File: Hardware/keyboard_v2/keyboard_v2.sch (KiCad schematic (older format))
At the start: 21 parts, among them J1 Conn_01x08_Male, SW1 SW_Push, SW2 SW_Push, SW3 SW_Push, SW4 SW_Push, SW5 SW_Push, SW6 SW_Push, U1 74HC14

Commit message: Распаян модуль keyboard_v2/
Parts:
- C2, C3, C4, C5, C6, C7: footprint Capacitor_SMD:C_0805_2012Metric_Pad1.18x1.45mm_HandSolder -> Capacitor_SMD:C_1206_3216Metric_Pad1.33x1.80mm_HandSolder
- SW1, SW2, SW3, SW4, SW5, SW6: footprint Button_Switch_SMD:SW_SPST_SMD_6.4_3.7 -> Button_Switch_SMD:SW_SPST_SMD_6.4_3.7_v2
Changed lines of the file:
@@
 F 0 "C2" H 3665 2046 50  0000 L CNN
 F 1 "C" H 3665 1955 50  0000 L CNN
-F 2 "Capacitor_SMD:C_0805_2012Metric_Pad1.18x1.45mm_HandSolder" H 3588 1850 50  0001 C CNN
+F 2 "Capacitor_SMD:C_1206_3216Metric_Pad1.33x1.80mm_HandSolder" H 3588 1850 50  0001 C CNN
 F 3 "~" H 3550 2000 50  0001 C CNN
 	1    3550 2000
@@
 F 0 "C3" H 3665 3546 50  0000 L CNN
 F 1 "C" H 3665 3455 50  0000 L CNN
-F 2 "Capacitor_SMD:C_0805_2012Metric_Pad1.18x1.45mm_HandSolder" H 3588 3350 50  0001 C CNN
+F 2 "Capacitor_SMD:C_1206_3216Metric_Pad1.33x1.80mm_HandSolder" H 3588 3350 50  0001 C CNN
 F 3 "~" H 3550 3500 50  0001 C CNN
 	1    3550 3500
@@
 F 0 "C4" H 3665 5146 50  0000 L CNN
 F 1 "C" H 3665 5055 50  0000 L CNN
-F 2 "Capacitor_SMD:C_0805_2012Metric_Pad1.18x1.45mm_HandSolder" H 3588 4950 50  0001 C CNN
+F 2 "Capacitor_SMD:C_1206_3216Metric_Pad1.33x1.80mm_HandSolder" H 3588 4950 50  0001 C CNN
 F 3 "~" H 3550 5100 50  0001 C CNN
 	1    3550 5100
@@
 F 0 "C5" H 6115 2046 50  0000 L CNN
 F 1 "C" H 6115 1955 50  0000 L CNN
-F 2 "Capacitor_SMD:C_0805_2012Metric_Pad1.18x1.45mm_HandSolder" H 6038 1850 50  0001 C CNN
+F 2 "Capacitor_SMD:C_1206_3216Metric_Pad1.33x1.80mm_HandSolder" H 6038 1850 50  0001 C CNN
 F 3 "~" H 6000 2000 50  0001 C CNN
 	1    6000 2000
@@
 F 0 "C6" H 6115 3546 50  0000 L CNN
 F 1 "C" H 6115 3455 50  0000 L CNN
-F 2 "Capacitor_SMD:C_0805_2012Metric_Pad1.18x1.45mm_HandSolder" H 6038 3350 50  0001 C CNN
+F 2 "Capacitor_SMD:C_1206_3216Metric_Pad1.33x1.80mm_HandSolder" H 6038 3350 50  0001 C CNN
 F 3 "~" H 6000 3500 50  0001 C CNN
 	1    6000 3500
@@
 F 0 "C7" H 6115 5046 50  0000 L CNN
 F 1 "C" H 6115 4955 50  0000 L CNN
-F 2 "Capacitor_SMD:C_0805_2012Metric_Pad1.18x1.45mm_HandSolder" H 6038 4850 50  0001 C CNN
+F 2 "Capacitor_SMD:C_1206_3216Metric_Pad1.33x1.80mm_HandSolder" H 6038 4850 50  0001 C CNN
 F 3 "~" H 6000 5000 50  0001 C CNN
 	1    6000 5000
@@
 F 0 "SW1" V 3804 2098 50  0000 L CNN
 F 1 "SW_Push" V 3895 2098 50  0000 L CNN
-F 2 "Button_Switch_SMD:SW_SPST_SMD_6.4_3.7" H 3850 2150 50  0001 C CNN
+F 2 "Button_Switch_SMD:SW_SPST_SMD_6.4_3.7_v2" H 3850 2150 50  0001 C CNN
 F 3 "~" H 3850 2150 50  0001 C CNN
 	1    3850 1950
@@
 F 0 "SW2" V 3804 3548 50  0000 L CNN
 F 1 "SW_Push" V 3895 3548 50  0000 L CNN
-F 2 "Button_Switch_SMD:SW_SPST_SMD_6.4_3.7" H 3850 3600 50  0001 C CNN
+F 2 "Button_Switch_SMD:SW_SPST_SMD_6.4_3.7_v2" H 3850 3600 50  0001 C CNN
 F 3 "~" H 3850 3600 50  0001 C CNN
 	1    3850 3400
@@
 F 0 "SW3" V 3804 5148 50  0000 L CNN
 F 1 "SW_Push" V 3895 5148 50  0000 L CNN
-F 2 "Button_Switch_SMD:SW_SPST_SMD_6.4_3.7" H 3850 5200 50  0001 C CNN
+F 2 "Button_Switch_SMD:SW_SPST_SMD_6.4_3.7_v2" H 3850 5200 50  0001 C CNN
 F 3 "~" H 3850 5200 50  0001 C CNN
 	1    3850 5000
@@
 F 0 "SW4" V 6254 2048 50  0000 L CNN
 F 1 "SW_Push" V 6345 2048 50  0000 L CNN
-F 2 "Button_Switch_SMD:SW_SPST_SMD_6.4_3.7" H 6300 2100 50  0001 C CNN
+F 2 "Button_Switch_SMD:SW_SPST_SMD_6.4_3.7_v2" H 6300 2100 50  0001 C CNN
 F 3 "~" H 6300 2100 50  0001 C CNN
 	1    6300 1900
@@
 F 0 "SW5" V 6254 3548 50  0000 L CNN
 F 1 "SW_Push" V 6345 3548 50  0000 L CNN
-F 2 "Button_Switch_SMD:SW_SPST_SMD_6.4_3.7" H 6300 3600 50  0001 C CNN
+F 2 "Button_Switch_SMD:SW_SPST_SMD_6.4_3.7_v2" H 6300 3600 50  0001 C CNN
 F 3 "~" H 6300 3600 50  0001 C CNN
 	1    6300 3400
@@
 F 0 "SW6" V 6254 5048 50  0000 L CNN
 F 1 "SW_Push" V 6345 5048 50  0000 L CNN
-F 2 "Button_Switch_SMD:SW_SPST_SMD_6.4_3.7" H 6300 5100 50  0001 C CNN
+F 2 "Button_Switch_SMD:SW_SPST_SMD_6.4_3.7_v2" H 6300 5100 50  0001 C CNN
 F 3 "~" H 6300 5100 50  0001 C CNN
 	1    6300 4900

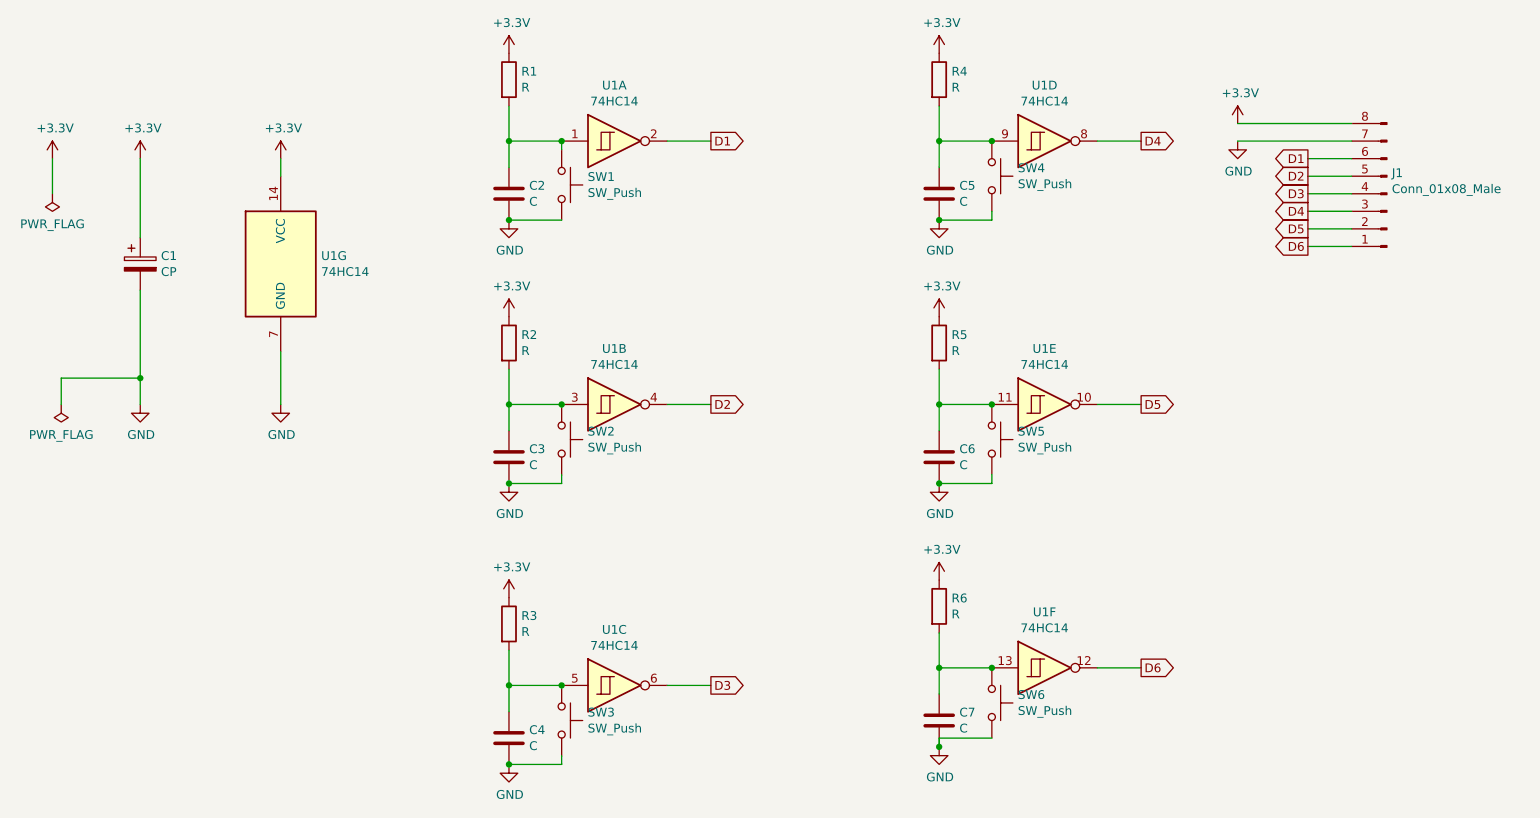
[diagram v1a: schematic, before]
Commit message: Распаян и протестирован модуль клавиатуры keyboard_v3/. Можно приступить к доработке основного приложения
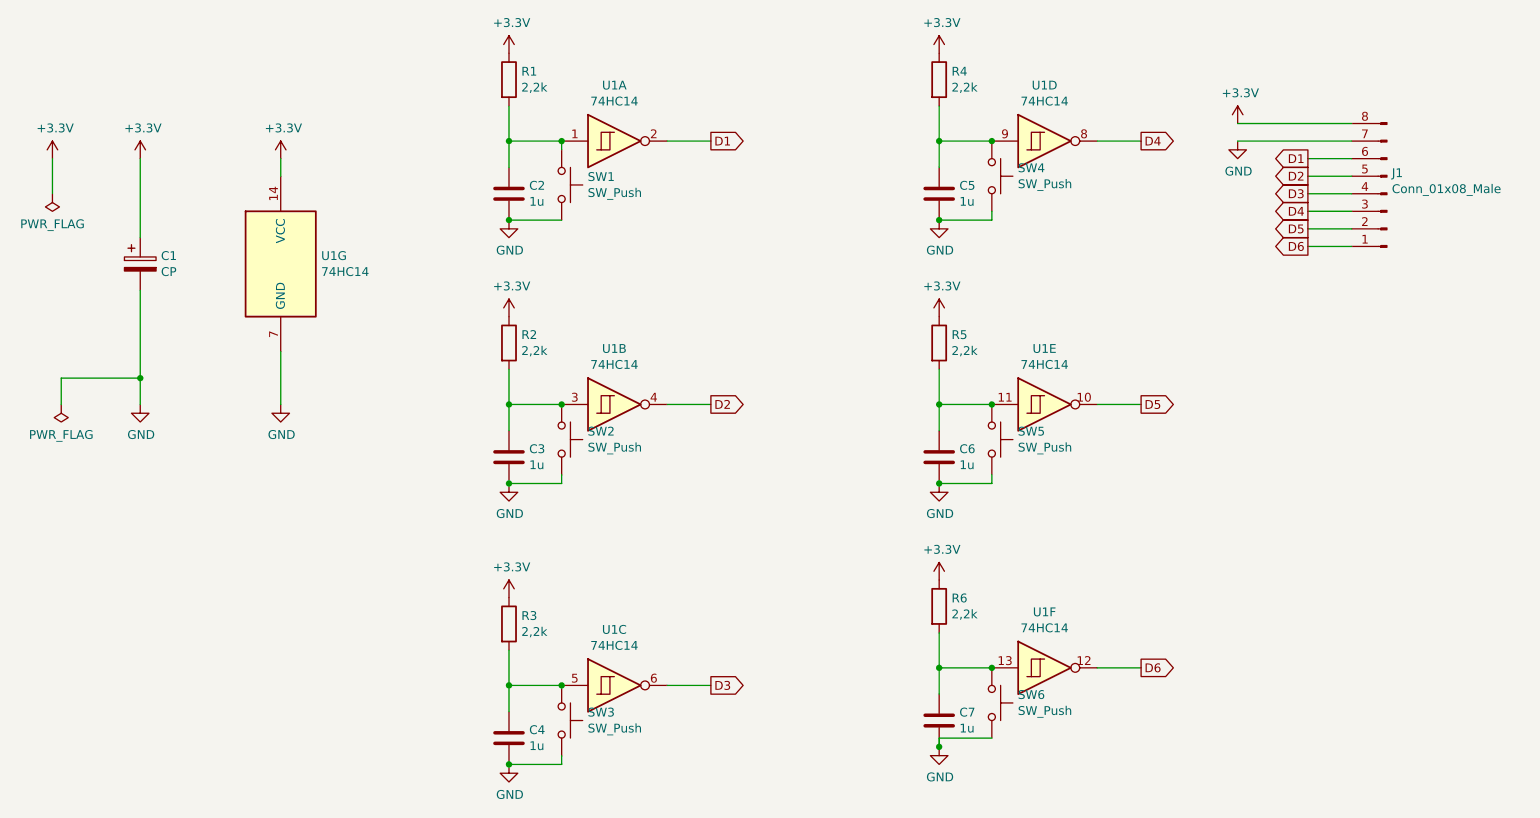
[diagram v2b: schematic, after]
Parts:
- C2, C3, C4, C5, C6, C7: value C -> 1u
- R1, R2, R3, R4, R5, R6: value R -> 2,2k
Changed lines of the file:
@@
 P 3550 1350
 F 0 "R1" H 3620 1396 50  0000 L CNN
-F 1 "R" H 3620 1305 50  0000 L CNN
+F 1 "2,2k" H 3620 1305 50  0000 L CNN
 F 2 "Resistor_SMD:R_1206_3216Metric_Pad1.30x1.75mm_HandSolder" V 3480 1350 50  0001 C CNN
 F 3 "~" H 3550 1350 50  0001 C CNN
@@
 P 3550 2000
 F 0 "C2" H 3665 2046 50  0000 L CNN
-F 1 "C" H 3665 1955 50  0000 L CNN
+F 1 "1u" H 3665 1955 50  0000 L CNN
 F 2 "Capacitor_SMD:C_1206_3216Metric_Pad1.33x1.80mm_HandSolder" H 3588 1850 50  0001 C CNN
 F 3 "~" H 3550 2000 50  0001 C CNN
@@
 P 3550 2850
 F 0 "R2" H 3620 2896 50  0000 L CNN
-F 1 "R" H 3620 2805 50  0000 L CNN
+F 1 "2,2k" H 3620 2805 50  0000 L CNN
 F 2 "Resistor_SMD:R_1206_3216Metric_Pad1.30x1.75mm_HandSolder" V 3480 2850 50  0001 C CNN
 F 3 "~" H 3550 2850 50  0001 C CNN
@@
 P 3550 3500
 F 0 "C3" H 3665 3546 50  0000 L CNN
-F 1 "C" H 3665 3455 50  0000 L CNN
+F 1 "1u" H 3665 3455 50  0000 L CNN
 F 2 "Capacitor_SMD:C_1206_3216Metric_Pad1.33x1.80mm_HandSolder" H 3588 3350 50  0001 C CNN
 F 3 "~" H 3550 3500 50  0001 C CNN
@@
 P 3550 4450
 F 0 "R3" H 3620 4496 50  0000 L CNN
-F 1 "R" H 3620 4405 50  0000 L CNN
+F 1 "2,2k" H 3620 4405 50  0000 L CNN
 F 2 "Resistor_SMD:R_1206_3216Metric_Pad1.30x1.75mm_HandSolder" V 3480 4450 50  0001 C CNN
 F 3 "~" H 3550 4450 50  0001 C CNN
@@
 P 3550 5100
 F 0 "C4" H 3665 5146 50  0000 L CNN
-F 1 "C" H 3665 5055 50  0000 L CNN
+F 1 "1u" H 3665 5055 50  0000 L CNN
 F 2 "Capacitor_SMD:C_1206_3216Metric_Pad1.33x1.80mm_HandSolder" H 3588 4950 50  0001 C CNN
 F 3 "~" H 3550 5100 50  0001 C CNN
@@
 P 6000 1350
 F 0 "R4" H 6070 1396 50  0000 L CNN
-F 1 "R" H 6070 1305 50  0000 L CNN
+F 1 "2,2k" H 6070 1305 50  0000 L CNN
 F 2 "Resistor_SMD:R_1206_3216Metric_Pad1.30x1.75mm_HandSolder" V 5930 1350 50  0001 C CNN
 F 3 "~" H 6000 1350 50  0001 C CNN
@@
 P 6000 2000
 F 0 "C5" H 6115 2046 50  0000 L CNN
-F 1 "C" H 6115 1955 50  0000 L CNN
+F 1 "1u" H 6115 1955 50  0000 L CNN
 F 2 "Capacitor_SMD:C_1206_3216Metric_Pad1.33x1.80mm_HandSolder" H 6038 1850 50  0001 C CNN
 F 3 "~" H 6000 2000 50  0001 C CNN
@@
 P 6000 2850
 F 0 "R5" H 6070 2896 50  0000 L CNN
-F 1 "R" H 6070 2805 50  0000 L CNN
+F 1 "2,2k" H 6070 2805 50  0000 L CNN
 F 2 "Resistor_SMD:R_1206_3216Metric_Pad1.30x1.75mm_HandSolder" V 5930 2850 50  0001 C CNN
 F 3 "~" H 6000 2850 50  0001 C CNN
@@
 P 6000 3500
 F 0 "C6" H 6115 3546 50  0000 L CNN
-F 1 "C" H 6115 3455 50  0000 L CNN
+F 1 "1u" H 6115 3455 50  0000 L CNN
 F 2 "Capacitor_SMD:C_1206_3216Metric_Pad1.33x1.80mm_HandSolder" H 6038 3350 50  0001 C CNN
 F 3 "~" H 6000 3500 50  0001 C CNN
@@
 P 6000 4350
 F 0 "R6" H 6070 4396 50  0000 L CNN
-F 1 "R" H 6070 4305 50  0000 L CNN
+F 1 "2,2k" H 6070 4305 50  0000 L CNN
 F 2 "Resistor_SMD:R_1206_3216Metric_Pad1.30x1.75mm_HandSolder" V 5930 4350 50  0001 C CNN
 F 3 "~" H 6000 4350 50  0001 C CNN
@@
 P 6000 5000
 F 0 "C7" H 6115 5046 50  0000 L CNN
-F 1 "C" H 6115 4955 50  0000 L CNN
+F 1 "1u" H 6115 4955 50  0000 L CNN
 F 2 "Capacitor_SMD:C_1206_3216Metric_Pad1.33x1.80mm_HandSolder" H 6038 4850 50  0001 C CNN
 F 3 "~" H 6000 5000 50  0001 C CNN
